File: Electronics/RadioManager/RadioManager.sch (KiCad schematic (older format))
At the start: 10 parts, among them J1 RJ45-MAG-LED, J10 JUMPER-NO, J2 RJ45-MAG-LED, J3 RJ45-MAG-LED, J4 RJ45-MAG-LED, J5 RJ45-MAG-LED, J6 CONN-DC, J7 JUMPER-NO, J8 JUMPER-NO, J9 JUMPER-NO

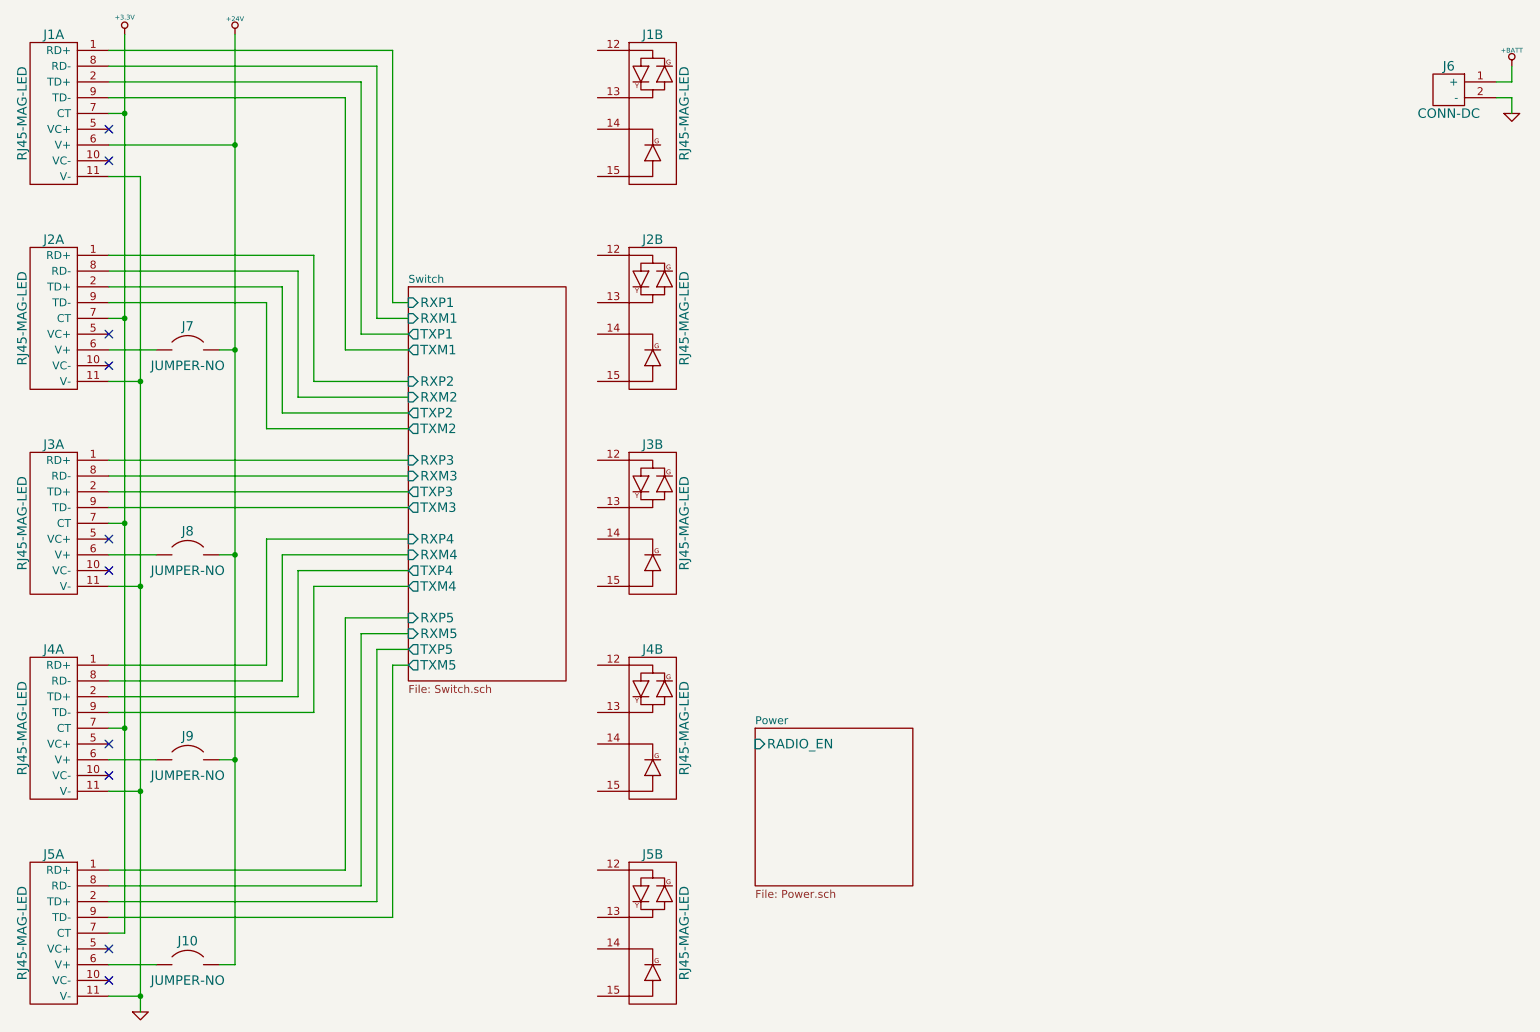
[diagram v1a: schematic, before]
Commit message: Connect LEDs
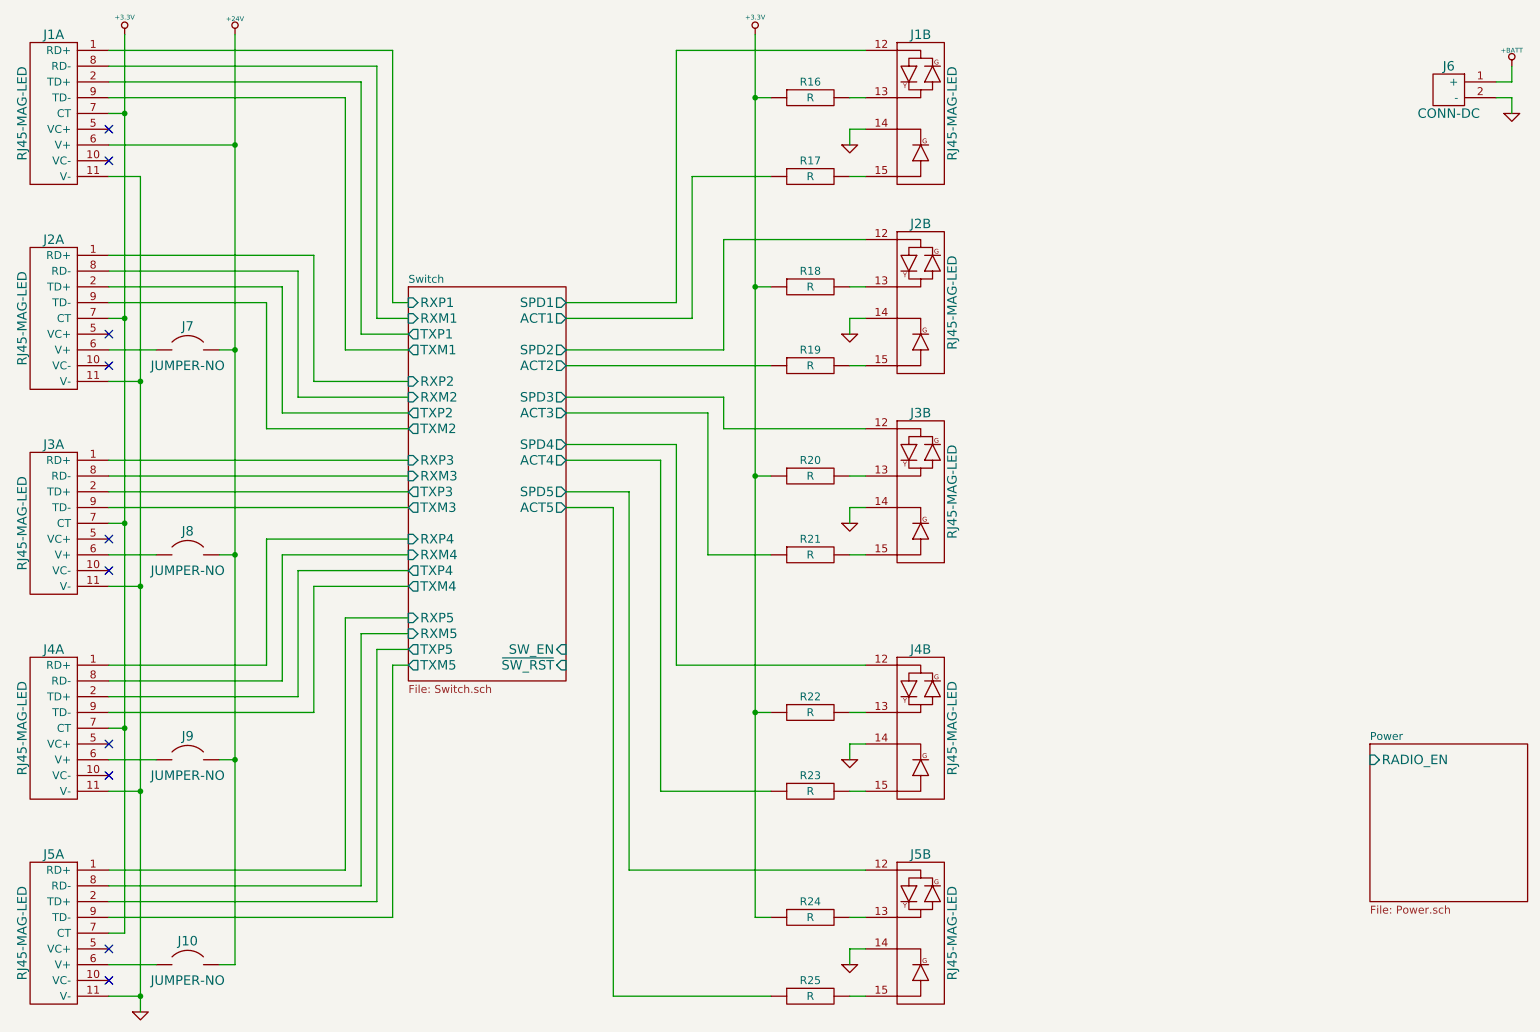
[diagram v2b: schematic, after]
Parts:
- added R16, R17, R18, R19, R20, R21, R22, R23, R24, R25: R, ~, symbol R
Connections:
- net +3.3V: now also R16.1, R18.1, R20.1, R22.1, R24.1
- net GND: now also J1.14, J2.14, J3.14, J4.14, J5.14
- net Switch/SPD1: now reaches J1.12
- net at J1.13: now also R16.2
- net at J1.15: now also R17.2
- net Switch/SPD2: now reaches J2.12
- net at J2.13: now also R18.2
- net at J2.15: now also R19.2
- net Switch/SPD3: now reaches J3.12
- net at J3.13: now also R20.2
- net at J3.15: now also R21.2
- net Switch/SPD4: now reaches J4.12
- net at J4.13: now also R22.2
- net at J4.15: now also R23.2
- net Switch/SPD5: now reaches J5.12
- net at J5.13: now also R24.2
- net at J5.15: now also R25.2
- new net Switch/ACT1: R17.1
- new net Switch/ACT2: R19.1
- new net Switch/ACT3: R21.1
- new net Switch/ACT4: R23.1
- new net Switch/ACT5: R25.1
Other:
- moved on the sheet: J1B, J2B, J3B, J4B, J5B

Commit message: Resistor values
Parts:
- R16, R17, R18, R19, R20, R21, R22, R23, R24, R25: value R -> 120; Distributor Part No (none) -> RHM120CGCT-ND; MFR Name (none) -> Rohm; MFR Part No (none) -> MCR03ERTJ121; Power W -> 1/10W; Tolerance % -> 5%
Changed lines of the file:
@@
 Sheet 1 3
 Title ""
-Date "3 oct 2014"
+Date "5 oct 2014"
 Rev ""
 Comp ""
@@
 $EndComp
 $Comp
-L R R17
-U 1 1 541FD7D2
-P 5950 1800
-F 0 "R17" H 5950 1900 50  0000 C CNN
-F 1 "R" H 5950 1800 50  0000 C CNN
-F 2 "~" H 5950 1800 60  0000 C CNN
-F 3 "~" H 5950 1800 60  0000 C CNN
-F 4 "W" H 5950 1700 50  0001 C CNN "Power"
-F 5 "%" H 5950 1600 50  0001 C CNN "Tolerance"
-	1    5950 1800
-	1    0    0    -1
-$EndComp
-$Comp
 L GND #PWR06
 U 1 1 541FD7FD
@@
 P 5950 1300
 F 0 "R16" H 5950 1400 50  0000 C CNN
-F 1 "R" H 5950 1300 50  0000 C CNN
+F 1 "120" H 5950 1300 50  0000 C CNN
 F 2 "~" H 5950 1300 60  0000 C CNN
 F 3 "~" H 5950 1300 60  0000 C CNN
-F 4 "W" H 5950 1200 50  0001 C CNN "Power"
-F 5 "%" H 5950 1100 50  0001 C CNN "Tolerance"
+F 4 "Rohm" H 5950 1300 60  0001 C CNN "MFR Name"
+F 5 "MCR03ERTJ121" H 5950 1300 60  0001 C CNN "MFR Part No"
+F 6 "RHM120CGCT-ND" H 5950 1300 60  0001 C CNN "Distributor Part No"
+F 7 "1/10W" H 5950 1200 50  0001 C CNN "Power"
+F 8 "5%" H 5950 1100 50  0001 C CNN "Tolerance"
 	1    5950 1300
-	1    0    0    -1
-$EndComp
-$Comp
-L R R18
-U 1 1 542012F3
-P 5950 2500
-F 0 "R18" H 5950 2600 50  0000 C CNN
-F 1 "R" H 5950 2500 50  0000 C CNN
-F 2 "~" H 5950 2500 60  0000 C CNN
-F 3 "~" H 5950 2500 60  0000 C CNN
-F 4 "W" H 5950 2400 50  0001 C CNN "Power"
-F 5 "%" H 5950 2300 50  0001 C CNN "Tolerance"
-	1    5950 2500
-	1    0    0    -1
-$EndComp
-$Comp
-L R R19
-U 1 1 542012FB
-P 5950 3000
-F 0 "R19" H 5950 3100 50  0000 C CNN
-F 1 "R" H 5950 3000 50  0000 C CNN
-F 2 "~" H 5950 3000 60  0000 C CNN
-F 3 "~" H 5950 3000 60  0000 C CNN
-F 4 "W" H 5950 2900 50  0001 C CNN "Power"
-F 5 "%" H 5950 2800 50  0001 C CNN "Tolerance"
-	1    5950 3000
-	1    0    0    -1
-$EndComp
-$Comp
-L R R20
-U 1 1 54201366
-P 5950 3700
-F 0 "R20" H 5950 3800 50  0000 C CNN
-F 1 "R" H 5950 3700 50  0000 C CNN
-F 2 "~" H 5950 3700 60  0000 C CNN
-F 3 "~" H 5950 3700 60  0000 C CNN
-F 4 "W" H 5950 3600 50  0001 C CNN "Power"
-F 5 "%" H 5950 3500 50  0001 C CNN "Tolerance"
-	1    5950 3700
-	1    0    0    -1
-$EndComp
-$Comp
-L R R21
-U 1 1 5420136E
-P 5950 4200
-F 0 "R21" H 5950 4300 50  0000 C CNN
-F 1 "R" H 5950 4200 50  0000 C CNN
-F 2 "~" H 5950 4200 60  0000 C CNN
-F 3 "~" H 5950 4200 60  0000 C CNN
-F 4 "W" H 5950 4100 50  0001 C CNN "Power"
-F 5 "%" H 5950 4000 50  0001 C CNN "Tolerance"
-	1    5950 4200
-	1    0    0    -1
-$EndComp
-$Comp
-L R R25
-U 1 1 54201565
-P 5950 7000
-F 0 "R25" H 5950 7100 50  0000 C CNN
-F 1 "R" H 5950 7000 50  0000 C CNN
-F 2 "~" H 5950 7000 60  0000 C CNN
-F 3 "~" H 5950 7000 60  0000 C CNN
-F 4 "W" H 5950 6900 50  0001 C CNN "Power"
-F 5 "%" H 5950 6800 50  0001 C CNN "Tolerance"
-	1    5950 7000
-	1    0    0    -1
-$EndComp
-$Comp
-L R R24
-U 1 1 542015D0
-P 5950 6500
-F 0 "R24" H 5950 6600 50  0000 C CNN
-F 1 "R" H 5950 6500 50  0000 C CNN
-F 2 "~" H 5950 6500 60  0000 C CNN
-F 3 "~" H 5950 6500 60  0000 C CNN
-F 4 "W" H 5950 6400 50  0001 C CNN "Power"
-F 5 "%" H 5950 6300 50  0001 C CNN "Tolerance"
-	1    5950 6500
-	1    0    0    -1
-$EndComp
-$Comp
-L R R23
-U 1 1 542015D8
-P 5950 5700
-F 0 "R23" H 5950 5800 50  0000 C CNN
-F 1 "R" H 5950 5700 50  0000 C CNN
-F 2 "~" H 5950 5700 60  0000 C CNN
-F 3 "~" H 5950 5700 60  0000 C CNN
-F 4 "W" H 5950 5600 50  0001 C CNN "Power"
-F 5 "%" H 5950 5500 50  0001 C CNN "Tolerance"
-	1    5950 5700
-	1    0    0    -1
-$EndComp
-$Comp
-L R R22
-U 1 1 542015E0
-P 5950 5200
-F 0 "R22" H 5950 5300 50  0000 C CNN
-F 1 "R" H 5950 5200 50  0000 C CNN
-F 2 "~" H 5950 5200 60  0000 C CNN
-F 3 "~" H 5950 5200 60  0000 C CNN
-F 4 "W" H 5950 5100 50  0001 C CNN "Power"
-F 5 "%" H 5950 5000 50  0001 C CNN "Tolerance"
-	1    5950 5200
 	1    0    0    -1
 $EndComp
@@
 Wire Wire Line
 	4400 3900 4700 3900
+$Comp
+L R R17
+U 1 1 543104DB
+P 5950 1800
+F 0 "R17" H 5950 1900 50  0000 C CNN
+F 1 "120" H 5950 1800 50  0000 C CNN
+F 2 "~" H 5950 1800 60  0000 C CNN
+F 3 "~" H 5950 1800 60  0000 C CNN
+F 4 "Rohm" H 5950 1800 60  0001 C CNN "MFR Name"
+F 5 "MCR03ERTJ121" H 5950 1800 60  0001 C CNN "MFR Part No"
+F 6 "RHM120CGCT-ND" H 5950 1800 60  0001 C CNN "Distributor Part No"
+F 7 "1/10W" H 5950 1700 50  0001 C CNN "Power"
+F 8 "5%" H 5950 1600 50  0001 C CNN "Tolerance"
+	1    5950 1800
+	1    0    0    -1
+$EndComp
+$Comp
+L R R18
+U 1 1 543104E6
+P 5950 2500
+F 0 "R18" H 5950 2600 50  0000 C CNN
+F 1 "120" H 5950 2500 50  0000 C CNN
+F 2 "~" H 5950 2500 60  0000 C CNN
+F 3 "~" H 5950 2500 60  0000 C CNN
+F 4 "Rohm" H 5950 2500 60  0001 C CNN "MFR Name"
+F 5 "MCR03ERTJ121" H 5950 2500 60  0001 C CNN "MFR Part No"
+F 6 "RHM120CGCT-ND" H 5950 2500 60  0001 C CNN "Distributor Part No"
+F 7 "1/10W" H 5950 2400 50  0001 C CNN "Power"
+F 8 "5%" H 5950 2300 50  0001 C CNN "Tolerance"
+	1    5950 2500
+	1    0    0    -1
+$EndComp
+$Comp
+L R R19
+U 1 1 543105B7
+P 5950 3000
+F 0 "R19" H 5950 3100 50  0000 C CNN
+F 1 "120" H 5950 3000 50  0000 C CNN
+F 2 "~" H 5950 3000 60  0000 C CNN
+F 3 "~" H 5950 3000 60  0000 C CNN
+F 4 "Rohm" H 5950 3000 60  0001 C CNN "MFR Name"
+F 5 "MCR03ERTJ121" H 5950 3000 60  0001 C CNN "MFR Part No"
+F 6 "RHM120CGCT-ND" H 5950 3000 60  0001 C CNN "Distributor Part No"
+F 7 "1/10W" H 5950 2900 50  0001 C CNN "Power"
+F 8 "5%" H 5950 2800 50  0001 C CNN "Tolerance"
+	1    5950 3000
+	1    0    0    -1
+$EndComp
+$Comp
+L R R20
+U 1 1 5431074E
+P 5950 3700
+F 0 "R20" H 5950 3800 50  0000 C CNN
+F 1 "120" H 5950 3700 50  0000 C CNN
+F 2 "~" H 5950 3700 60  0000 C CNN
+F 3 "~" H 5950 3700 60  0000 C CNN
+F 4 "Rohm" H 5950 3700 60  0001 C CNN "MFR Name"
+F 5 "MCR03ERTJ121" H 5950 3700 60  0001 C CNN "MFR Part No"
+F 6 "RHM120CGCT-ND" H 5950 3700 60  0001 C CNN "Distributor Part No"
+F 7 "1/10W" H 5950 3600 50  0001 C CNN "Power"
+F 8 "5%" H 5950 3500 50  0001 C CNN "Tolerance"
+	1    5950 3700
+	1    0    0    -1
+$EndComp
+$Comp
+L R R21
+U 1 1 54310759
+P 5950 4200
+F 0 "R21" H 5950 4300 50  0000 C CNN
+F 1 "120" H 5950 4200 50  0000 C CNN
+F 2 "~" H 5950 4200 60  0000 C CNN
+F 3 "~" H 5950 4200 60  0000 C CNN
+F 4 "Rohm" H 5950 4200 60  0001 C CNN "MFR Name"
+F 5 "MCR03ERTJ121" H 5950 4200 60  0001 C CNN "MFR Part No"
+F 6 "RHM120CGCT-ND" H 5950 4200 60  0001 C CNN "Distributor Part No"
+F 7 "1/10W" H 5950 4100 50  0001 C CNN "Power"
+F 8 "5%" H 5950 4000 50  0001 C CNN "Tolerance"
+	1    5950 4200
+	1    0    0    -1
+$EndComp
+$Comp
+L R R22
+U 1 1 54310764
+P 5950 5200
+F 0 "R22" H 5950 5300 50  0000 C CNN
+F 1 "120" H 5950 5200 50  0000 C CNN
+F 2 "~" H 5950 5200 60  0000 C CNN
+F 3 "~" H 5950 5200 60  0000 C CNN
+F 4 "Rohm" H 5950 5200 60  0001 C CNN "MFR Name"
+F 5 "MCR03ERTJ121" H 5950 5200 60  0001 C CNN "MFR Part No"
+F 6 "RHM120CGCT-ND" H 5950 5200 60  0001 C CNN "Distributor Part No"
+F 7 "1/10W" H 5950 5100 50  0001 C CNN "Power"
+F 8 "5%" H 5950 5000 50  0001 C CNN "Tolerance"
+	1    5950 5200
+	1    0    0    -1
+$EndComp
+$Comp
+L R R23
+U 1 1 543108FB
+P 5950 5700
+F 0 "R23" H 5950 5800 50  0000 C CNN
+F 1 "120" H 5950 5700 50  0000 C CNN
+F 2 "~" H 5950 5700 60  0000 C CNN
+F 3 "~" H 5950 5700 60  0000 C CNN
+F 4 "Rohm" H 5950 5700 60  0001 C CNN "MFR Name"
+F 5 "MCR03ERTJ121" H 5950 5700 60  0001 C CNN "MFR Part No"
+F 6 "RHM120CGCT-ND" H 5950 5700 60  0001 C CNN "Distributor Part No"
+F 7 "1/10W" H 5950 5600 50  0001 C CNN "Power"
+F 8 "5%" H 5950 5500 50  0001 C CNN "Tolerance"
+	1    5950 5700
+	1    0    0    -1
+$EndComp
+$Comp
+L R R24
+U 1 1 54310906
+P 5950 6500
+F 0 "R24" H 5950 6600 50  0000 C CNN
+F 1 "120" H 5950 6500 50  0000 C CNN
+F 2 "~" H 5950 6500 60  0000 C CNN
+F 3 "~" H 5950 6500 60  0000 C CNN
+F 4 "Rohm" H 5950 6500 60  0001 C CNN "MFR Name"
+F 5 "MCR03ERTJ121" H 5950 6500 60  0001 C CNN "MFR Part No"
+F 6 "RHM120CGCT-ND" H 5950 6500 60  0001 C CNN "Distributor Part No"
+F 7 "1/10W" H 5950 6400 50  0001 C CNN "Power"
+F 8 "5%" H 5950 6300 50  0001 C CNN "Tolerance"
+	1    5950 6500
+	1    0    0    -1
+$EndComp
+$Comp
+L R R25
+U 1 1 54310911
+P 5950 7000
+F 0 "R25" H 5950 7100 50  0000 C CNN
+F 1 "120" H 5950 7000 50  0000 C CNN
+F 2 "~" H 5950 7000 60  0000 C CNN
+F 3 "~" H 5950 7000 60  0000 C CNN
+F 4 "Rohm" H 5950 7000 60  0001 C CNN "MFR Name"
+F 5 "MCR03ERTJ121" H 5950 7000 60  0001 C CNN "MFR Part No"
+F 6 "RHM120CGCT-ND" H 5950 7000 60  0001 C CNN "Distributor Part No"
+F 7 "1/10W" H 5950 6900 50  0001 C CNN "Power"
+F 8 "5%" H 5950 6800 50  0001 C CNN "Tolerance"
+	1    5950 7000
+	1    0    0    -1
+$EndComp
 $EndSCHEMATC
